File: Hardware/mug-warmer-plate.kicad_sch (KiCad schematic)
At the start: 30 parts, among them Q1 IRLZ44N, SW1 SW_DIP_x01, U1 LM35-NEB, U2 ATtiny85-20P

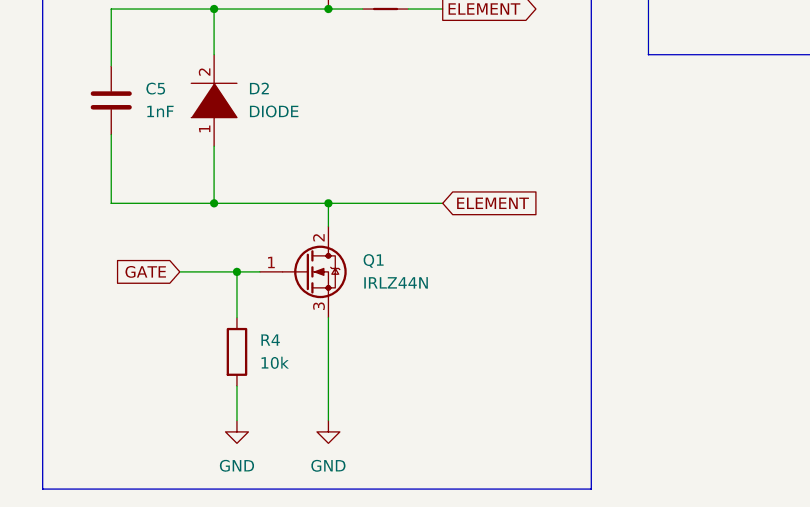
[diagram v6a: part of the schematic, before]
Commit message: Initial PCB placement
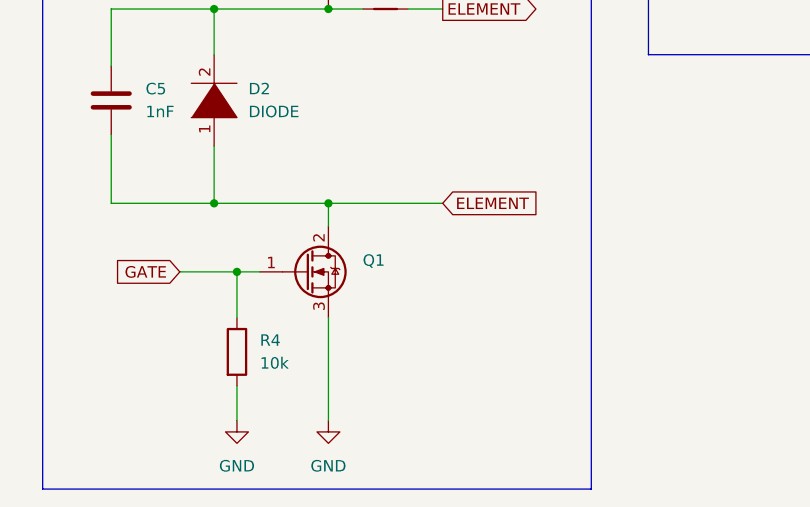
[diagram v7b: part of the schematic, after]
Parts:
- NT1: footprint (none) -> NetTie:NetTie-2_SMD_Pad0.5mm
- Q1: value IRLZ44N -> (none); footprint Package_TO_SOT_THT:TO-220-3_Vertical -> (none)
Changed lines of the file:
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@@
     (property "Reference" "NT1" (id 0) (at 140.97 135.89 0))
     (property "Value" "" (id 1) (at 140.97 138.43 0))
-    (property "Footprint" "" (id 2) (at 140.97 140.97 0)
+    (property "Footprint" "NetTie:NetTie-2_SMD_Pad0.5mm" (id 2) (at 140.97 140.97 0)
       (effects (font (size 1.27 1.27)) hide)
     )
@@
       (effects (font (size 1.27 1.27)) (justify left))
     )
-    (property "Value" "IRLZ44N" (id 1) (at 138.43 171.4499 0)
-      (effects (font (size 1.27 1.27)) (justify left))
-    )
-    (property "Footprint" "Package_TO_SOT_THT:TO-220-3_Vertical" (id 2) (at 138.43 172.085 0)
+    (property "Value" "" (id 1) (at 138.43 171.4499 0)
+      (effects (font (size 1.27 1.27)) (justify left))
+    )
+    (property "Footprint" "" (id 2) (at 138.43 172.085 0)
       (effects (font (size 1.27 1.27) italic) (justify left) hide)
     )
@@
     )
     (path "/214e1aa8-c026-40c3-9c5c-83401d2e77f3"
-      (reference "NT1") (unit 1) (value "NetTie_2") (footprint "NetTie:NetTie-2_SMD_Pad2.0mm")
+      (reference "NT1") (unit 1) (value "NetTie_2") (footprint "NetTie:NetTie-2_SMD_Pad0.5mm")
     )
     (path "/c229fabb-c04a-4bb3-af27-16bead0c0502"

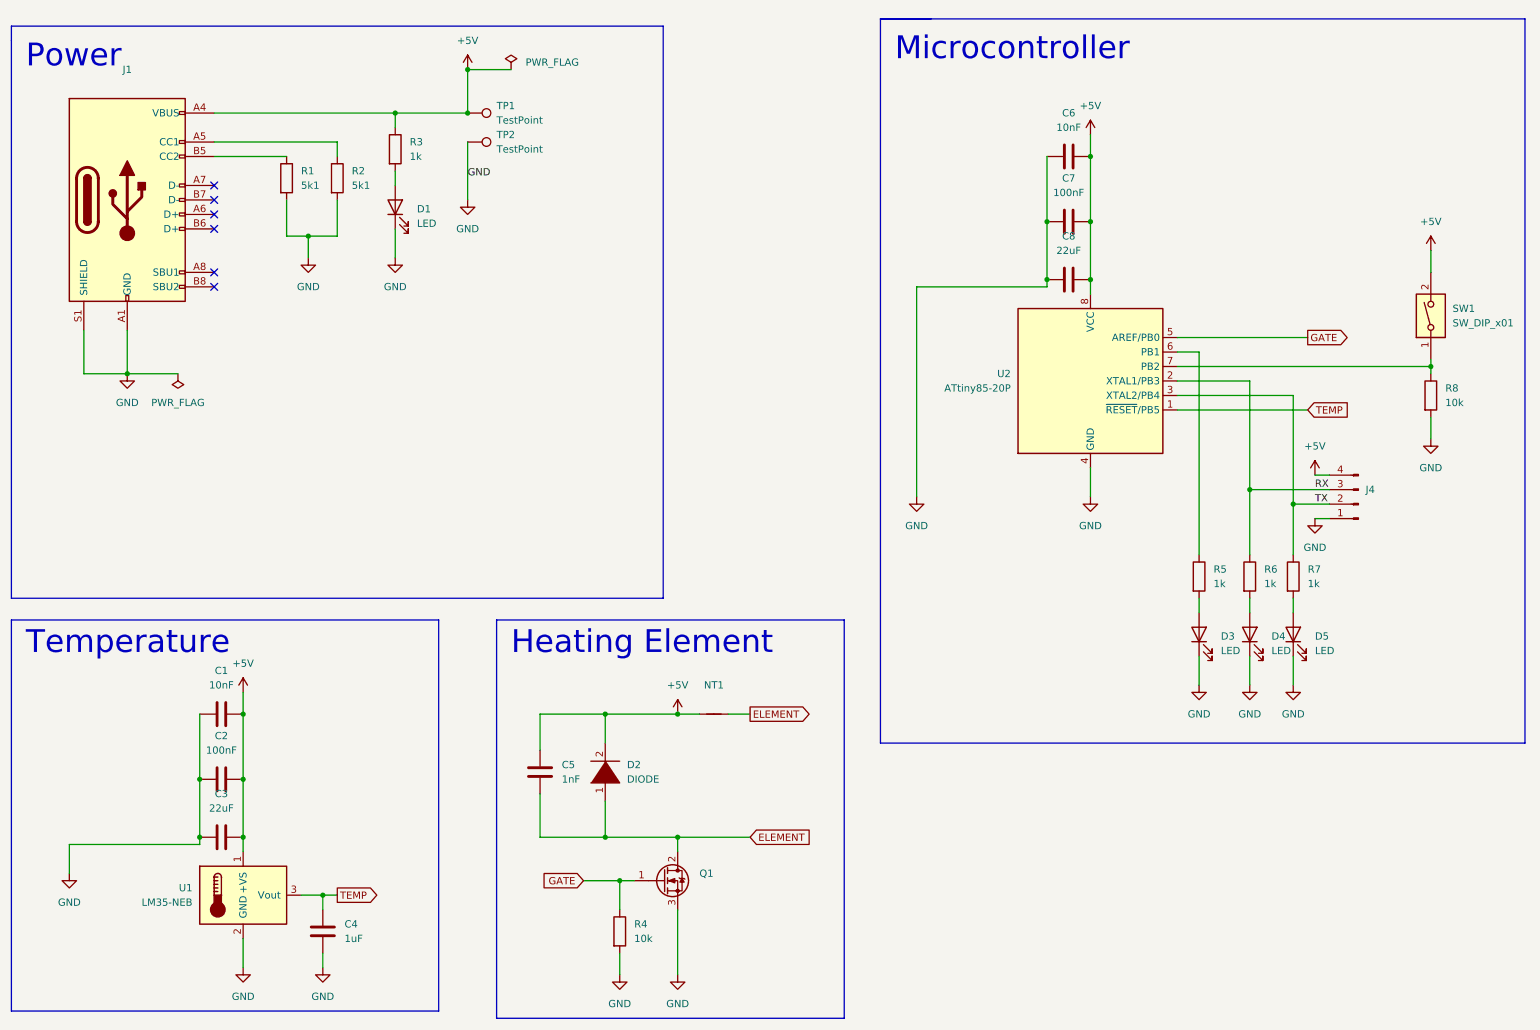
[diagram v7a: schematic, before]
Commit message: Complete routing and pass DRC check
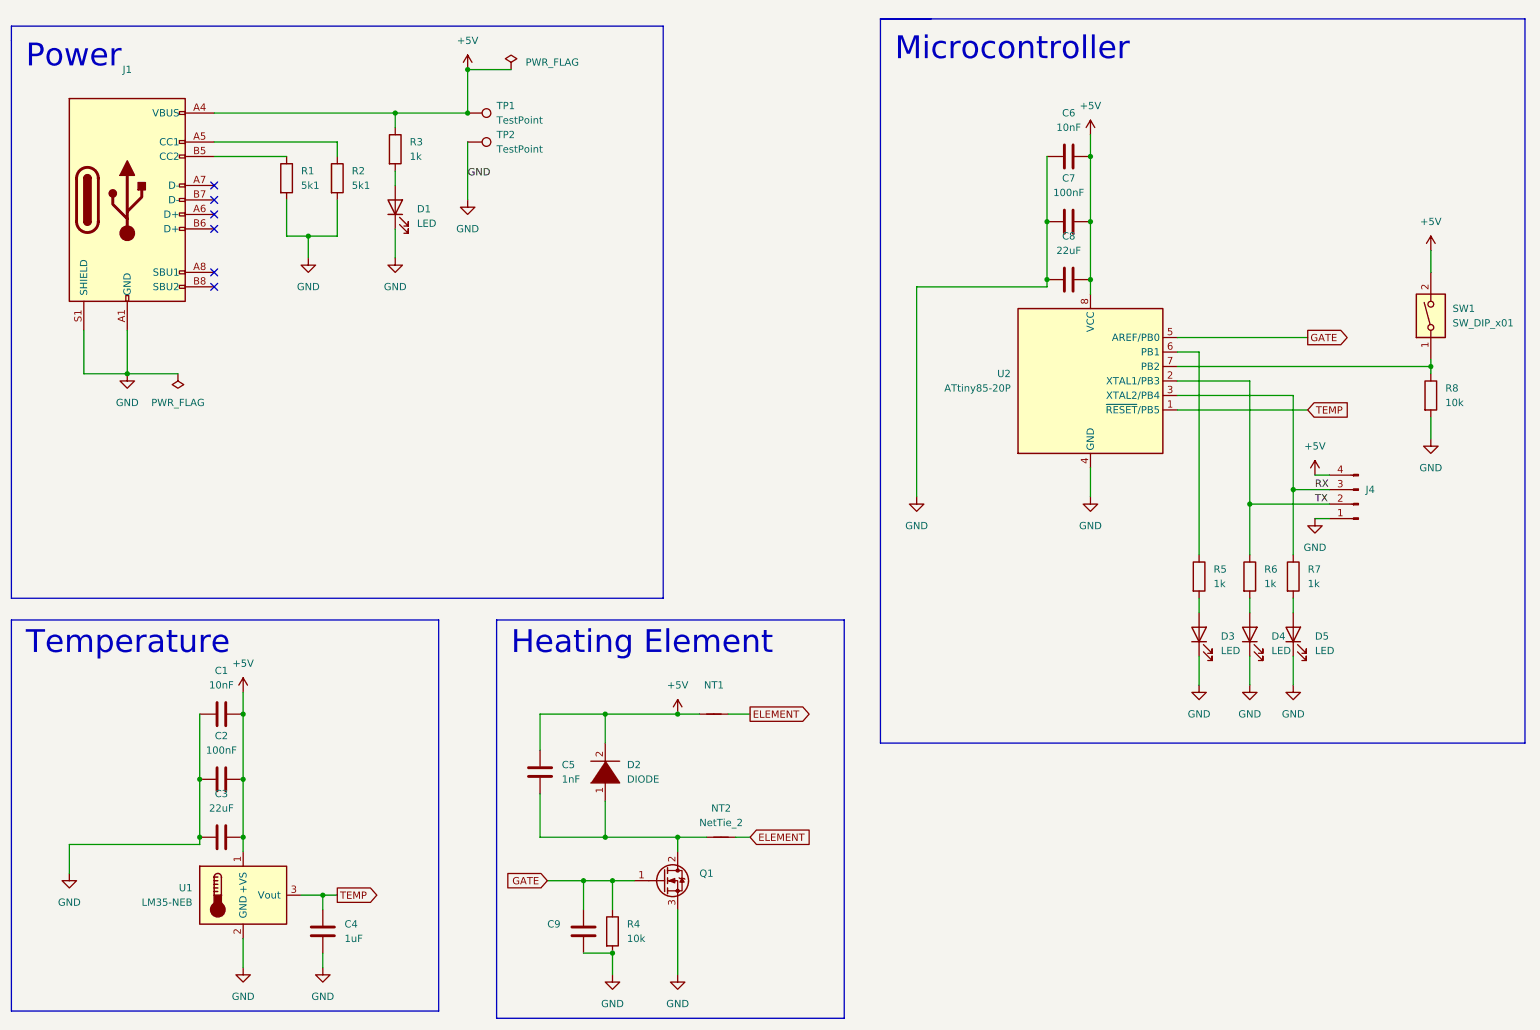
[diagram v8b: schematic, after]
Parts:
- added C9: (no value), symbol Device:C
- added NT2: NetTie_2, NetTie:NetTie-2_SMD_Pad0.5mm, symbol Device:NetTie_2
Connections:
- net ELEMENT: now also NT2.2; no longer C5.1, D2.1 (K), Q1.2 (D)
- net GATE: now also C9.2
- net GND: now also C9.1
- net RX: now also R7.1, U2.3 (XTAL2/PB4); no longer R6.1, U2.2 (XTAL1/PB3)
- net TX: now also R6.1, U2.2 (XTAL1/PB3); no longer R7.1, U2.3 (XTAL2/PB4)
- new net: C5.1, D2.1 (K), NT2.1, Q1.2 (D)
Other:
- moved on the sheet: R4
